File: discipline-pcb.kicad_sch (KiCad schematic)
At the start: 198 parts, among them SW1 KEYSW, SW10 KEYSW, SW11 KEYSW, SW12 KEYSW, SW13 KEYSW, SW14 KEYSW, SW16 KEYSW, SW17 KEYSW, SW18 KEYSW, SW19 KEYSW, SW2 KEYSW, SW20 KEYSW, SW21 KEYSW, SW22 KEYSW, SW23 KEYSW, SW24 KEYSW, SW25 KEYSW, SW26 KEYSW, SW27 KEYSW, SW28 KEYSW, SW29 KEYSW, SW3 KEYSW, SW31 KEYSW, SW32 KEYSW, SW33 KEYSW, SW34 KEYSW, SW35 KEYSW, SW36 KEYSW, SW37 KEYSW, SW38 KEYSW, SW39 KEYSW, SW4 KEYSW, SW40 KEYSW, SW41 KEYSW, SW42 KEYSW, SW43 KEYSW, SW45 KEYSW, SW46 KEYSW, SW47 KEYSW, SW48 KEYSW, SW49 KEYSW, SW5 KEYSW, SW50 KEYSW, SW51 KEYSW, SW52 KEYSW, SW53 KEYSW, SW54 KEYSW, SW55 KEYSW, SW56 KEYSW, SW57 KEYSW, SW59 KEYSW, SW6 KEYSW, SW60 KEYSW, SW61 KEYSW, SW62 KEYSW, SW7 KEYSW, SW72 KEYSW, SW73 KEYSW, SW74 KEYSW, SW75 KEYSW, SW76 KEYSW, SW77 KEYSW, SW78 KEYSW, SW79 KEYSW, SW8 KEYSW, SW80 KEYSW, SW81 KEYSW, SW82 KEYSW, SW83 KEYSW, SW9 KEYSW, U1 SN74AHCT125N, U2 RP2040_Stamp

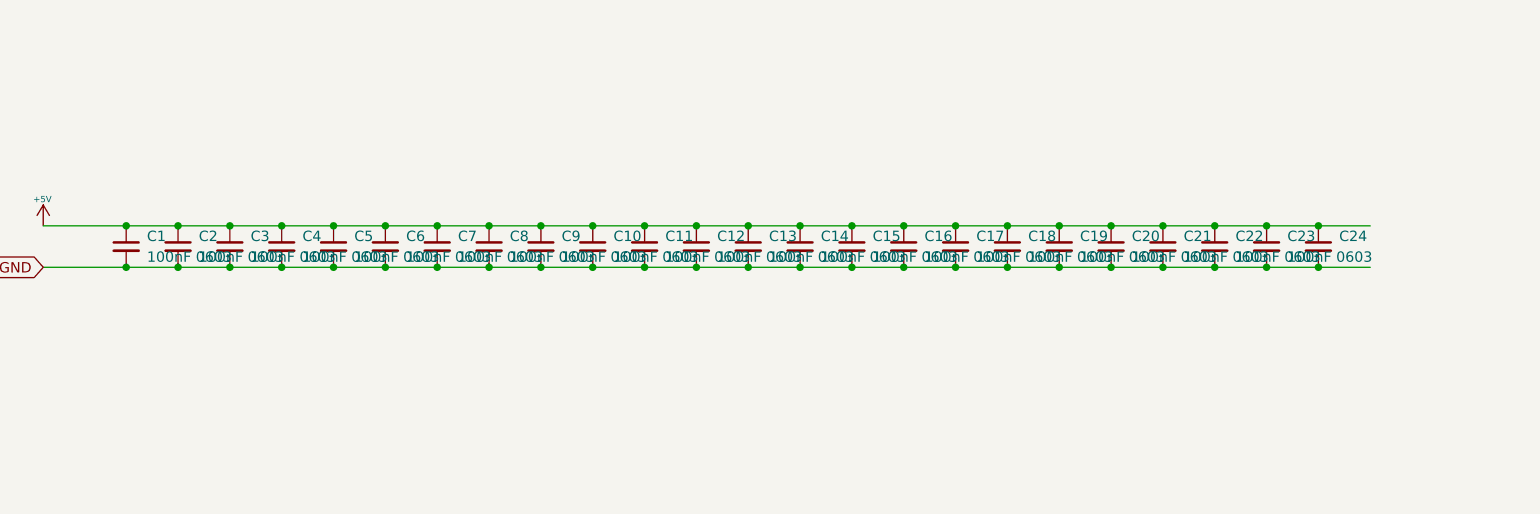
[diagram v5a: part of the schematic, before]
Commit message: move to 0805
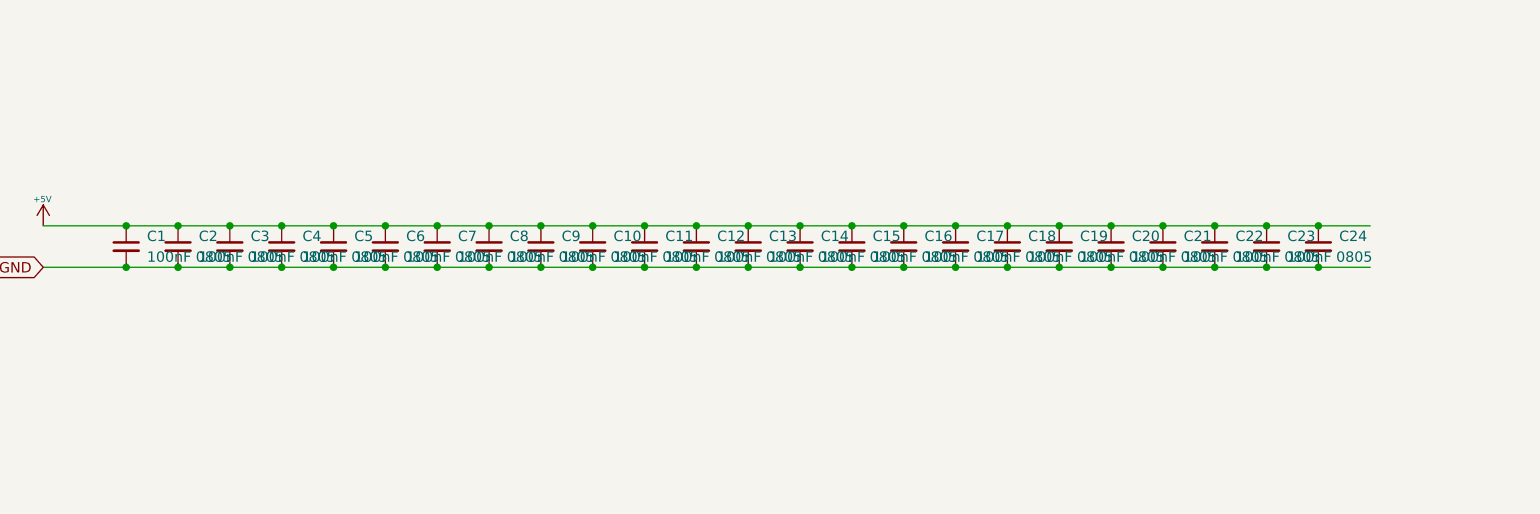
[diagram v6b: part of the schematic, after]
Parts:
- C1, C10, C11, C12, C13, C14, C15, C16, C17, C18, C19, C2, C20, C21, C22, C23, C24, C3, C4, C5, C6, C7, C8, C9: value 100nF 0603 -> 100nF 0805; footprint Capacitor_SMD:C_0603_1608Metric_Pad1.08x0.95mm_HandSolder -> Capacitor_SMD:C_0805_2012Metric_Pad1.18x1.45mm_HandSolder
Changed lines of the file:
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@@
 			)
 		)
-		(property "Value" "100nF 0603"
+		(property "Value" "100nF 0805"
 			(at 130.81 237.4962 0)
 			(effects
@@
 			)
 		)
-		(property "Footprint" "Capacitor_SMD:C_0603_1608Metric_Pad1.08x0.95mm_HandSolder"
+		(property "Footprint" "Capacitor_SMD:C_0805_2012Metric_Pad1.18x1.45mm_HandSolder"
 			(at 128.27 236.22 0)
 			(effects
@@
 			)
 		)
-		(property "Value" "100nF 0603"
+		(property "Value" "100nF 0805"
 			(at 41.91 237.4962 0)
 			(effects
@@
 			)
 		)
-		(property "Footprint" "Capacitor_SMD:C_0603_1608Metric_Pad1.08x0.95mm_HandSolder"
+		(property "Footprint" "Capacitor_SMD:C_0805_2012Metric_Pad1.18x1.45mm_HandSolder"
 			(at 39.37 236.22 0)
 			(effects
@@
 			)
 		)
-		(property "Value" "100nF 0603"
+		(property "Value" "100nF 0805"
 			(at 105.41 237.4962 0)
 			(effects
@@
 			)
 		)
-		(property "Footprint" "Capacitor_SMD:C_0603_1608Metric_Pad1.08x0.95mm_HandSolder"
+		(property "Footprint" "Capacitor_SMD:C_0805_2012Metric_Pad1.18x1.45mm_HandSolder"
 			(at 102.87 236.22 0)
 			(effects
@@
 			)
 		)
-		(property "Value" "100nF 0603"
+		(property "Value" "100nF 0805"
 			(at 67.31 237.4962 0)
 			(effects
@@
 			)
 		)
-		(property "Footprint" "Capacitor_SMD:C_0603_1608Metric_Pad1.08x0.95mm_HandSolder"
+		(property "Footprint" "Capacitor_SMD:C_0805_2012Metric_Pad1.18x1.45mm_HandSolder"
 			(at 64.77 236.22 0)
 			(effects
@@
 			)
 		)
-		(property "Value" "100nF 0603"
+		(property "Value" "100nF 0805"
 			(at 137.16 237.4962 0)
 			(effects
@@
 			)
 		)
-		(property "Footprint" "Capacitor_SMD:C_0603_1608Metric_Pad1.08x0.95mm_HandSolder"
+		(property "Footprint" "Capacitor_SMD:C_0805_2012Metric_Pad1.18x1.45mm_HandSolder"
 			(at 134.62 236.22 0)
 			(effects
@@
 			)
 		)
-		(property "Value" "100nF 0603"
+		(property "Value" "100nF 0805"
 			(at 48.26 237.4962 0)
 			(effects
@@
 			)
 		)
-		(property "Footprint" "Capacitor_SMD:C_0603_1608Metric_Pad1.08x0.95mm_HandSolder"
+		(property "Footprint" "Capacitor_SMD:C_0805_2012Metric_Pad1.18x1.45mm_HandSolder"
 			(at 45.72 236.22 0)
 			(effects
@@
 			)
 		)
-		(property "Value" "100nF 0603"
+		(property "Value" "100nF 0805"
 			(at 149.86 237.4962 0)
 			(effects
@@
 			)
 		)
-		(property "Footprint" "Capacitor_SMD:C_0603_1608Metric_Pad1.08x0.95mm_HandSolder"
+		(property "Footprint" "Capacitor_SMD:C_0805_2012Metric_Pad1.18x1.45mm_HandSolder"
 			(at 147.32 236.22 0)
 			(effects
@@
 			)
 		)
-		(property "Value" "100nF 0603"
+		(property "Value" "100nF 0805"
 			(at 156.21 237.4962 0)
 			(effects
@@
 			)
 		)
-		(property "Footprint" "Capacitor_SMD:C_0603_1608Metric_Pad1.08x0.95mm_HandSolder"
+		(property "Footprint" "Capacitor_SMD:C_0805_2012Metric_Pad1.18x1.45mm_HandSolder"
 			(at 153.67 236.22 0)
 			(effects
@@
 			)
 		)
-		(property "Value" "100nF 0603"
+		(property "Value" "100nF 0805"
 			(at 111.76 237.4962 0)
 			(effects
@@
 			)
 		)
-		(property "Footprint" "Capacitor_SMD:C_0603_1608Metric_Pad1.08x0.95mm_HandSolder"
+		(property "Footprint" "Capacitor_SMD:C_0805_2012Metric_Pad1.18x1.45mm_HandSolder"
 			(at 109.22 236.22 0)
 			(effects
@@
 			)
 		)
-		(property "Value" "100nF 0603"
+		(property "Value" "100nF 0805"
 			(at 175.26 237.4962 0)
 			(effects
@@
 			)
 		)
-		(property "Footprint" "Capacitor_SMD:C_0603_1608Metric_Pad1.08x0.95mm_HandSolder"
+		(property "Footprint" "Capacitor_SMD:C_0805_2012Metric_Pad1.18x1.45mm_HandSolder"
 			(at 172.72 236.22 0)
 			(effects
@@
 			)
 		)
-		(property "Value" "100nF 0603"
+		(property "Value" "100nF 0805"
 			(at 99.06 237.4962 0)
 			(effects
@@
 			)
 		)
-		(property "Footprint" "Capacitor_SMD:C_0603_1608Metric_Pad1.08x0.95mm_HandSolder"
+		(property "Footprint" "Capacitor_SMD:C_0805_2012Metric_Pad1.18x1.45mm_HandSolder"
 			(at 96.52 236.22 0)
 			(effects
@@
 			)
 		)
-		(property "Value" "100nF 0603"
+		(property "Value" "100nF 0805"
 			(at 118.11 237.4962 0)
 			(effects
@@
 			)
 		)
-		(property "Footprint" "Capacitor_SMD:C_0603_1608Metric_Pad1.08x0.95mm_HandSolder"
+		(property "Footprint" "Capacitor_SMD:C_0805_2012Metric_Pad1.18x1.45mm_HandSolder"
 			(at 115.57 236.22 0)
 			(effects
@@
 			)
 		)
-		(property "Value" "100nF 0603"
+		(property "Value" "100nF 0805"
 			(at 54.61 237.4962 0)
 			(effects
@@
 			)
 		)
-		(property "Footprint" "Capacitor_SMD:C_0603_1608Metric_Pad1.08x0.95mm_HandSolder"
+		(property "Footprint" "Capacitor_SMD:C_0805_2012Metric_Pad1.18x1.45mm_HandSolder"
 			(at 52.07 236.22 0)
 			(effects
@@
 			)
 		)
-		(property "Value" "100nF 0603"
+		(property "Value" "100nF 0805"
 			(at 80.01 237.4962 0)
 			(effects
@@
 			)
 		)
-		(property "Footprint" "Capacitor_SMD:C_0603_1608Metric_Pad1.08x0.95mm_HandSolder"
+		(property "Footprint" "Capacitor_SMD:C_0805_2012Metric_Pad1.18x1.45mm_HandSolder"
 			(at 77.47 236.22 0)
 			(effects
@@
 			)
 		)
-		(property "Value" "100nF 0603"
+		(property "Value" "100nF 0805"
 			(at 162.56 237.4962 0)
 			(effects
@@
 			)
 		)
-		(property "Footprint" "Capacitor_SMD:C_0603_1608Metric_Pad1.08x0.95mm_HandSolder"
+		(property "Footprint" "Capacitor_SMD:C_0805_2012Metric_Pad1.18x1.45mm_HandSolder"
 			(at 160.02 236.22 0)
 			(effects
@@
 			)
 		)
-		(property "Value" "100nF 0603"
+		(property "Value" "100nF 0805"
 			(at 168.91 237.4962 0)
 			(effects
@@
 			)
 		)
-		(property "Footprint" "Capacitor_SMD:C_0603_1608Metric_Pad1.08x0.95mm_HandSolder"
+		(property "Footprint" "Capacitor_SMD:C_0805_2012Metric_Pad1.18x1.45mm_HandSolder"
 			(at 166.37 236.22 0)
 			(effects
@@
 			)
 		)
-		(property "Value" "100nF 0603"
+		(property "Value" "100nF 0805"
 			(at 181.61 237.4962 0)
 			(effects
@@
 			)
 		)
-		(property "Footprint" "Capacitor_SMD:C_0603_1608Metric_Pad1.08x0.95mm_HandSolder"
+		(property "Footprint" "Capacitor_SMD:C_0805_2012Metric_Pad1.18x1.45mm_HandSolder"
 			(at 179.07 236.22 0)
 			(effects
@@
 			)
 		)
-		(property "Value" "100nF 0603"
+		(property "Value" "100nF 0805"
 			(at 35.56 237.4962 0)
 			(effects
@@
 			)
 		)
-		(property "Footprint" "Capacitor_SMD:C_0603_1608Metric_Pad1.08x0.95mm_HandSolder"
+		(property "Footprint" "Capacitor_SMD:C_0805_2012Metric_Pad1.18x1.45mm_HandSolder"
 			(at 33.02 236.22 0)
 			(effects
@@
 			)
 		)
-		(property "Value" "100nF 0603"
+		(property "Value" "100nF 0805"
 			(at 73.66 237.4962 0)
 			(effects
@@
 			)
 		)
-		(property "Footprint" "Capacitor_SMD:C_0603_1608Metric_Pad1.08x0.95mm_HandSolder"
+		(property "Footprint" "Capacitor_SMD:C_0805_2012Metric_Pad1.18x1.45mm_HandSolder"
 			(at 71.12 236.22 0)
 			(effects
@@
 			)
 		)
-		(property "Value" "100nF 0603"
+		(property "Value" "100nF 0805"
 			(at 124.46 237.4962 0)
 			(effects
@@
 			)
 		)
-		(property "Footprint" "Capacitor_SMD:C_0603_1608Metric_Pad1.08x0.95mm_HandSolder"
+		(property "Footprint" "Capacitor_SMD:C_0805_2012Metric_Pad1.18x1.45mm_HandSolder"
 			(at 121.92 236.22 0)
 			(effects
@@
 			)
 		)
-		(property "Value" "100nF 0603"
+		(property "Value" "100nF 0805"
 			(at 143.51 237.4962 0)
 			(effects
@@
 			)
 		)
-		(property "Footprint" "Capacitor_SMD:C_0603_1608Metric_Pad1.08x0.95mm_HandSolder"
+		(property "Footprint" "Capacitor_SMD:C_0805_2012Metric_Pad1.18x1.45mm_HandSolder"
 			(at 140.97 236.22 0)
 			(effects
@@
 			)
 		)
-		(property "Value" "100nF 0603"
+		(property "Value" "100nF 0805"
 			(at 60.96 237.4962 0)
 			(effects
@@
 			)
 		)
-		(property "Footprint" "Capacitor_SMD:C_0603_1608Metric_Pad1.08x0.95mm_HandSolder"
+		(property "Footprint" "Capacitor_SMD:C_0805_2012Metric_Pad1.18x1.45mm_HandSolder"
 			(at 58.42 236.22 0)
 			(effects
@@
 			)
 		)
-		(property "Value" "100nF 0603"
+		(property "Value" "100nF 0805"
 			(at 86.36 237.4962 0)
 			(effects
@@
 			)
 		)
-		(property "Footprint" "Capacitor_SMD:C_0603_1608Metric_Pad1.08x0.95mm_HandSolder"
+		(property "Footprint" "Capacitor_SMD:C_0805_2012Metric_Pad1.18x1.45mm_HandSolder"
 			(at 83.82 236.22 0)
 			(effects
@@
 			)
 		)
-		(property "Value" "100nF 0603"
+		(property "Value" "100nF 0805"
 			(at 92.71 237.4962 0)
 			(effects
@@
 			)
 		)
-		(property "Footprint" "Capacitor_SMD:C_0603_1608Metric_Pad1.08x0.95mm_HandSolder"
+		(property "Footprint" "Capacitor_SMD:C_0805_2012Metric_Pad1.18x1.45mm_HandSolder"
 			(at 90.17 236.22 0)
 			(effects
